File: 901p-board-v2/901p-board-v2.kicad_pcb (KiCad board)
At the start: 2 copper layers, 32 parts, among them J1 USB-C (14 pins), J2 DE15, J3 AO(+/-), Q1 PMOS, U1 HUSB238_xxxDD, U3 ESP32-S3-DevKitC, U4 MAX3232, U5 NHD-C0220BIZ, U6 TPS63060

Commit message: finish v2 board
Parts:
- added C16: 100nF, Capacitor_SMD:C_0805_2012Metric_Pad1.18x1.45mm_HandSolder, F.Cu at (123.6, 104.3)
- added G***: LOGO, footprints:HF_logo, F.Cu at (136.6, 125.3)
- added R8: 5.1kΩ, Resistor_SMD:R_0805_2012Metric_Pad1.20x1.40mm_HandSolder, F.Cu at (73.3, 105.9)
- added R9: 5.1kΩ, Resistor_SMD:R_0805_2012Metric_Pad1.20x1.40mm_HandSolder, F.Cu at (73.2, 110.6)
- J3: footprint Connector_PinHeader_1.00mm:PinHeader_1x02_P1.00mm_Vertical -> Connector_PinHeader_2.54mm:PinHeader_1x02_P2.54mm_Vertical
- moved U3 114.4 mm to (47.5, 79.0)
- moved C2 77.7 mm to (106.6, 112.7), turned to 180 degrees
- moved C4 76.9 mm to (107.6, 114.8), turned to 0 degrees
- moved C3 73.5 mm to (103.6, 113.9), turned to 90 degrees
- moved C5 71.0 mm to (101.1, 113.9), turned to 90 degrees
- moved L1 70.9 mm to (76.2, 119.8), turned to 90 degrees
- moved C15 70.6 mm to (78.8, 111.8), turned to 180 degrees
- moved C14 69.5 mm to (78.8, 113.9), turned to 180 degrees
- moved C13 68.5 mm to (78.8, 116.1), turned to 180 degrees
- moved C12 67.3 mm to (107.4, 126.6), turned to 180 degrees
- moved U4 66.8 mm to (103.2, 120.7), turned to -90 degrees
- moved R6 66.3 mm to (81.8, 112.8), turned to -90 degrees
- moved U6 64.6 mm to (80.8, 119.8), turned to 90 degrees
- moved R7 63.6 mm to (82.7, 115.7), turned to 0 degrees
- moved C11 63.6 mm to (80.8, 123.3), turned to 0 degrees
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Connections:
- C8 pad 1: +3.3V -> Net-(U5-VOUT)
- C8 pad 2: Net-(U5-VOUT) -> GND
- J1 pad A4: Net-(Q1-D) -> Net-(Q1-S)
- J1 pad A9: Net-(Q1-D) -> Net-(Q1-S)
- J1 pad B4: Net-(Q1-D) -> Net-(Q1-S)
- J1 pad B9: Net-(Q1-D) -> Net-(Q1-S)
- Q1 pad 1: Net-(Q1-D) -> VBUS
- Q1 pad 3: VBUS -> Net-(Q1-S)
- R1 pad 1: Net-(Q1-D) -> Net-(Q1-S)
- R4 pad 2: Net-(Q1-D) -> Net-(Q1-S)
- U3 pad 32: unconnected-(U3-GPIO35-Pad32) -> /SCL
- U3 pad 33: unconnected-(U3-GPIO36-Pad33) -> /SDA
- U3 pad 36: unconnected-(U3-GPIO39/MTCK-Pad36) -> /SER_TX
- U3 pad 37: unconnected-(U3-GPIO40/MTDO-Pad37) -> /SER_RX
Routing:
- net +3.3V: track 3.07 -> 132.3 mm
- net /SCL: track 1.16 -> 74.2 mm
- net /SDA: track 1.28 -> 74.0 mm
- net +5V: track 24.2 -> 79.1 mm
- net /SER_RX: track 0.00 -> 46.0 mm
- net /SER_TX: track 0.00 -> 43.9 mm
- net VBUS: track 2.20 -> 34.7 mm, vias 0 -> 1
- net /AO-: track 0.00 -> 26.7 mm
- net Net-(Q1-S): track 0.00 -> 18.0 mm
- net Net-(Q1-D): track 10.8 -> 0.00 mm
- net Net-(U4-T1OUT): track 0.00 -> 6.95 mm
- net Net-(U4-R1IN): track 0.00 -> 6.53 mm
- net Net-(Q1-G): track 10.3 -> 3.84 mm, vias 2 -> 0
- net /AO+: track 0.00 -> 4.55 mm
- net Net-(U1-VIN): track 5.37 -> 2.07 mm
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- added copper zone on F.Cu, net /SCL
- added copper zone on F.Cu, net /SDA
- added copper zone on B.Cu, net GND
- added copper zone on F.Cu, net GND
- added copper zone on F.Cu, net Net-(Q1-S)
- added copper zone on F.Cu, net Net-(U1-VIN)
- added copper zone on F.Cu, net Net-(U6-VAUX)
- removed copper zone on F.Cu, net Net-(Q1-D)
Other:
- board outline added: 104.7 x 74.6 mm

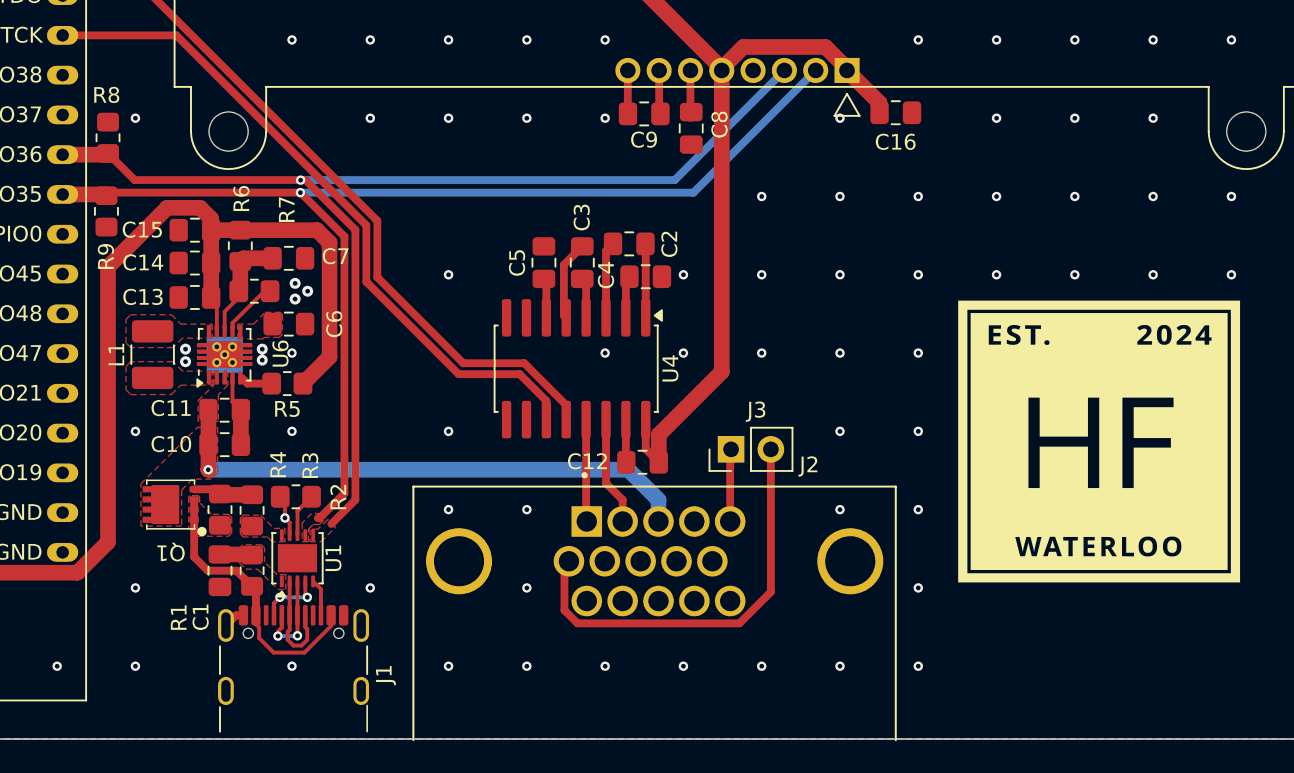
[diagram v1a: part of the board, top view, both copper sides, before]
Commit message: fix stitching vias, add more zones
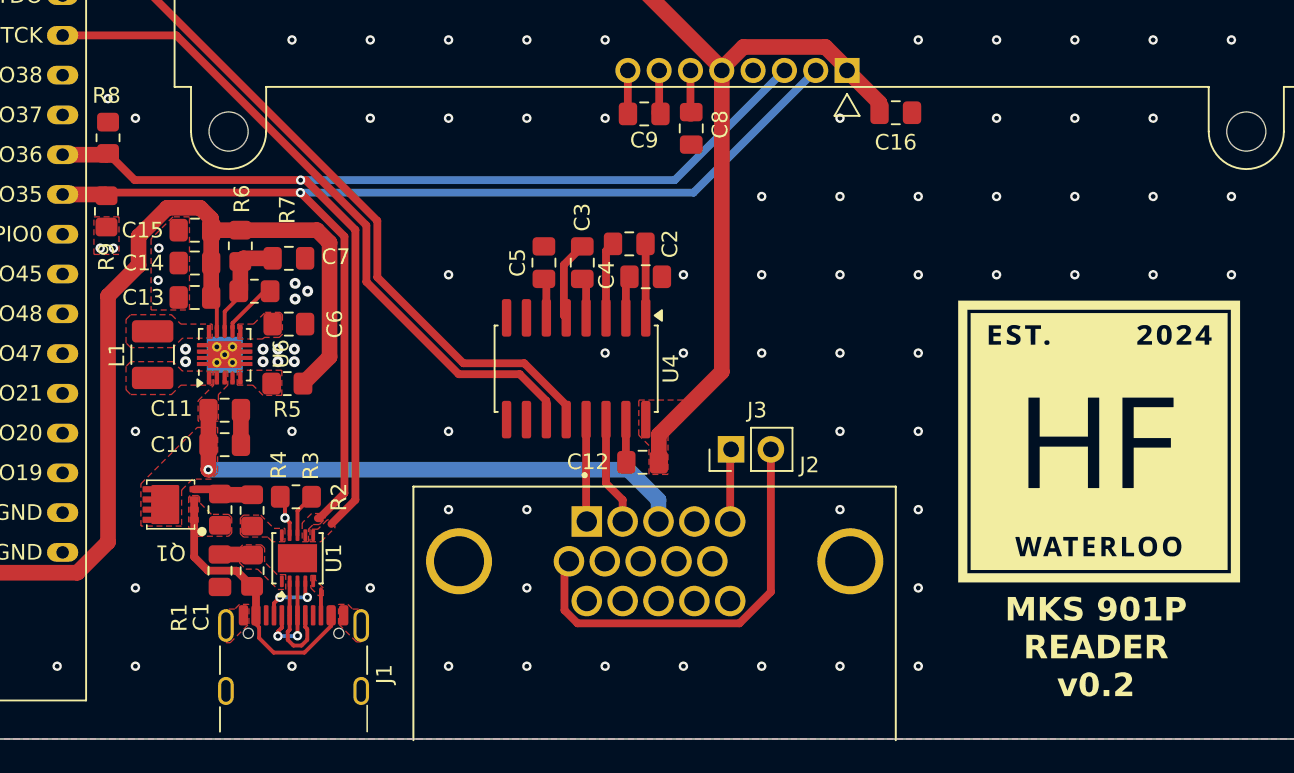
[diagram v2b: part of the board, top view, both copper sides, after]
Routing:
- net GND: track 14.8 -> 11.1 mm, vias 190 -> 198
- net +3.3V: track 132.3 -> 129.2 mm
- net Net-(U6-PG): track 2.06 -> 0.00 mm
- net Net-(J1-CC2): track 2.38 -> 1.67 mm
- added copper zone on F.Cu, net +3.3V
- added copper zone on F.Cu, net Net-(J1-CC2)
- added copper zone on F.Cu, net Net-(U6-PG)
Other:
- board text added: "MKS 901P READER v0.2"

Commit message: final review i think
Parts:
- turned R8 to -90 degrees
- turned R9 to 90 degrees
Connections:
- R8 pad 1: /SDA -> +3.3V
- R8 pad 2: GND -> /SDA
- R9 pad 1: /SCL -> +3.3V
- R9 pad 2: GND -> /SCL
- U4 pad 10: unconnected-(U4-T2IN-Pad10) -> GND
- U4 pad 8: unconnected-(U4-R2IN-Pad8) -> GND
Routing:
- net +3.3V: track 129.2 -> 153.7 mm, vias 0 -> 2
- net GND: track 11.1 -> 8.61 mm, vias 198 -> 15
- net Net-(J1-CC1): track 4.14 -> 3.31 mm
- added copper zone on F.Cu, net +5V
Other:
- board text added: "+"
- board text added: "-"
